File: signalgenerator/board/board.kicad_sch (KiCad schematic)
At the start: 20 parts, among them U1 MachXO2-1200, U5 74LVC04, U6 STLQ015M33R

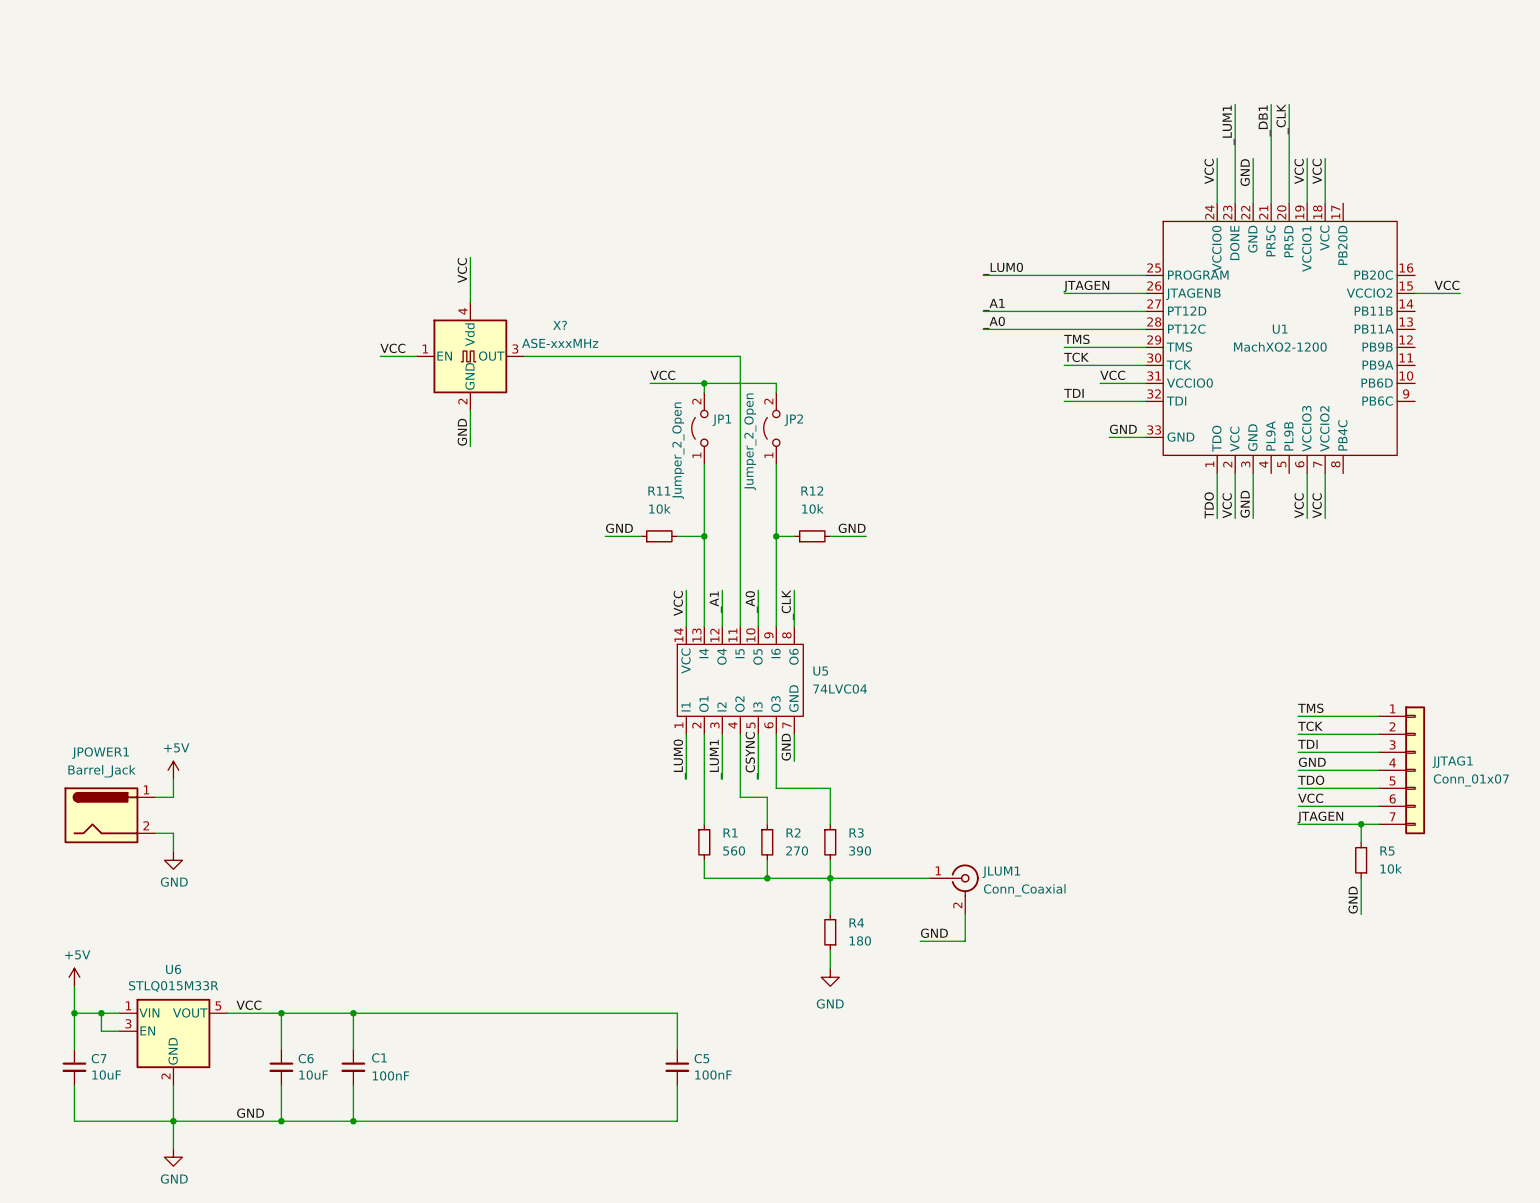
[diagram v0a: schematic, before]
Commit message: Reference board schematic
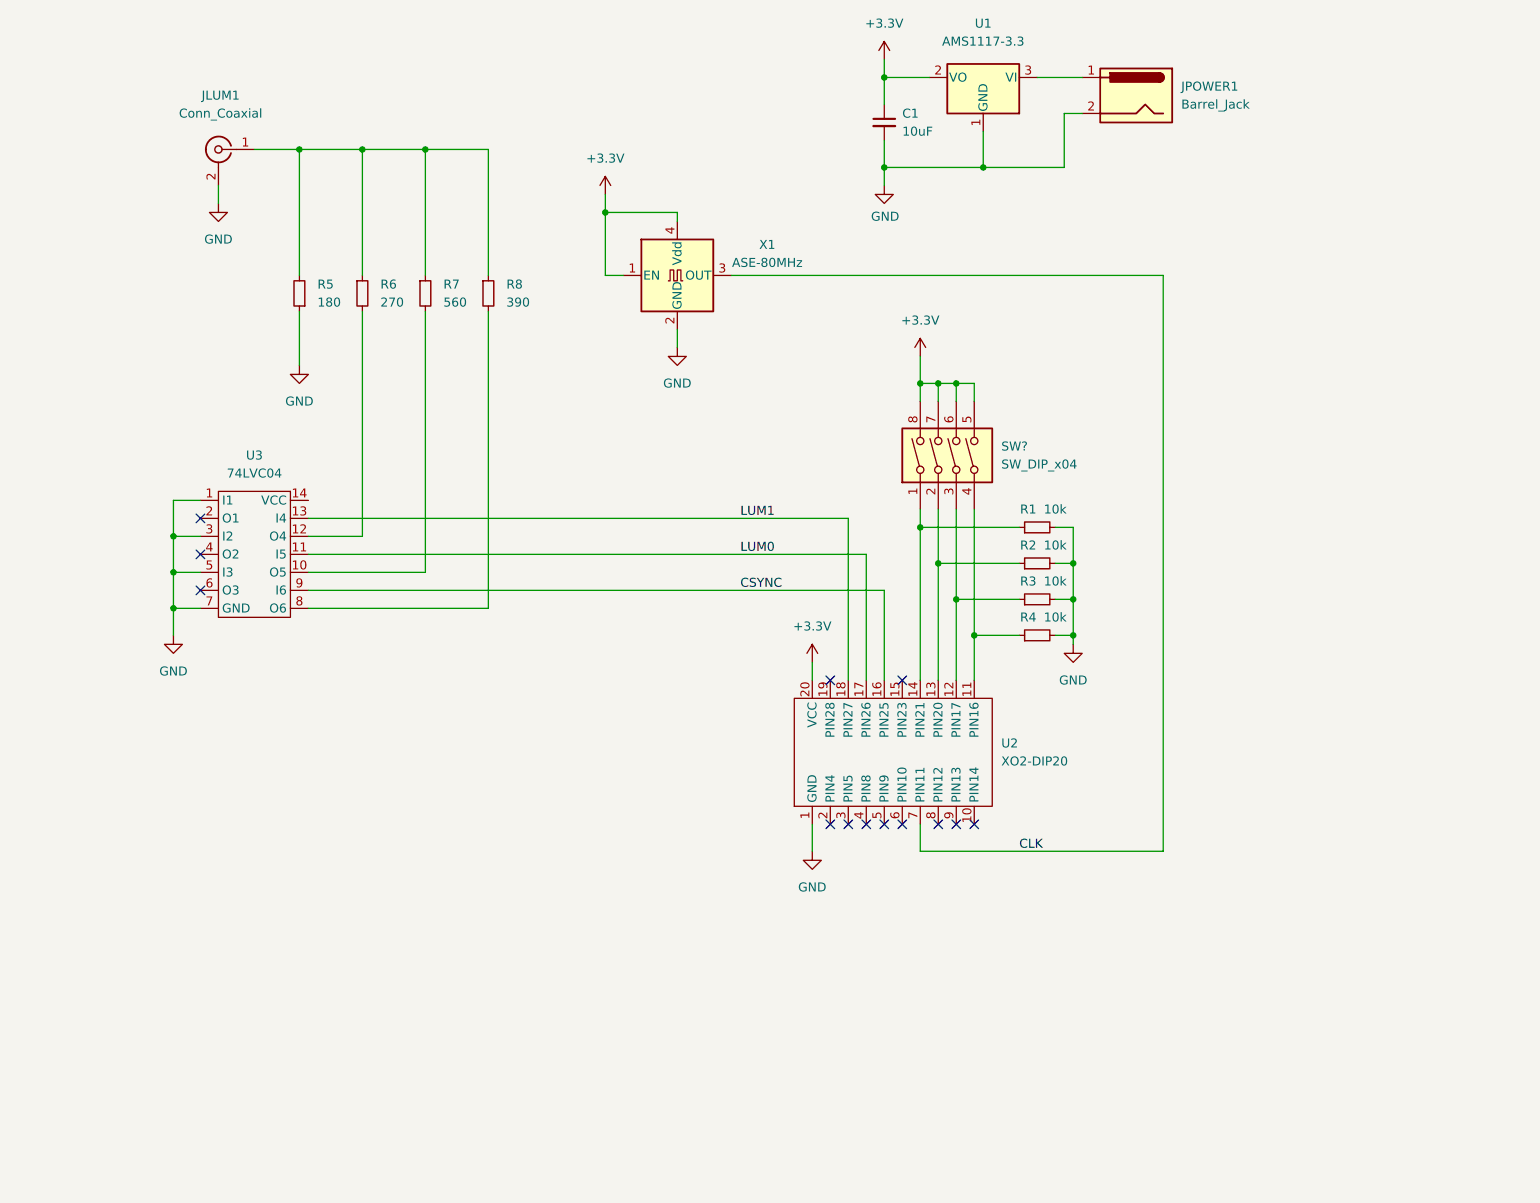
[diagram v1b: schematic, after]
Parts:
- removed C5: 100nF, Capacitor_SMD:C_0603_1608Metric, symbol Device:C_Small
- removed C6, C7: 10uF, Capacitor_SMD:C_0805_2012Metric, symbol Device:C_Small
- removed JJTAG1: Conn_01x07, Connector_PinHeader_2.54mm:PinHeader_1x07_P2.54mm_Vertical, symbol Connector_Generic:Conn_01x07
- removed JP1, JP2: Jumper_2_Open, symbol Jumper:Jumper_2_Open
- removed R11, R12: 10k, symbol Device:R_Small
- removed R5: 10k, Resistor_SMD:R_0805_2012Metric_Pad1.20x1.40mm_HandSolder, symbol Device:R_Small
- removed U1: MachXO2-1200, footprints:QFN-32-1EP_5x5mm_P0.5mm_EP3.1x3.1mm_ThermalVias, symbol Library:MachXO2-1200
- removed U6: STLQ015M33R, Package_TO_SOT_SMD:SOT-23-5, symbol vicboard-rescue:AP2127K-3.3-Regulator_Linear
- added R1, R2, R3, R4: 10k, symbol Device:R_Small
- added SW?: SW_DIP_x04, symbol Switch:SW_DIP_x04
- added U1: AMS1117-3.3, Package_TO_SOT_SMD:SOT-223-3_TabPin2, symbol Regulator_Linear:AMS1117-3.3
- added U2: XO2-DIP20, symbol Library:XO2-DIP20
- C1: value 100nF -> 10uF; footprint Capacitor_SMD:C_0603_1608Metric -> (none)
- X1: renamed from X?; value ASE-xxxMHz -> ASE-80MHz
- renumbered R4 to R5, R2 to R6, R1 to R7, R3 to R8, U5 to U3
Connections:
- net _CSYNC is gone; now on net GND: U3.5 (I3)
- net _LUM0 is gone; now on net GND: U3.1 (I1)
- net _LUM1 is gone; now on net GND: U3.3 (I2)
- net GND: now also R1.2, R2.2, R3.2, R4.2, U1.1 (GND), U2.1 (GND)
- net LUM1: now reaches U3.13 (I4)
- net LUM1: now also U2.18 (PIN27)
- net CLK: now reaches X1.3 (OUT)
- net CLK: now also U2.7 (PIN11); no longer U3.11 (I5)
- net at U3.2 (O1): no longer R7.1
- net at U3.4 (O2): no longer R6.1
- net at U3.6 (O3): no longer R8.1
- net CSYNC: now reaches U3.9 (I6)
- net CSYNC: now also U2.16 (PIN25)
- net +5V: no longer names the net of JPOWER1.1
- net +5V: now also U1.3 (VI)
- net VCC renamed +3.3V
- net +3.3V: now also SW?.5, SW?.6, SW?.7, SW?.8, U1.2 (VO), U2.20 (VCC); no longer U3.14 (VCC)
- net _A0: no longer names the net of U3.10 (O5)
- net _A0: now also R7.2
- net _A1: no longer names the net of U3.12 (O4)
- net _A1: now also R6.2
- net _CLK: no longer names the net of U3.8 (O6)
- net _CLK: now also R8.2
- new net: R4.1, SW?.4, U2.11 (PIN16)
- new net: R3.1, SW?.3, U2.12 (PIN17)
- new net: R2.1, SW?.2, U2.13 (PIN20)
- new net: R1.1, SW?.1, U2.14 (PIN21)
- new net: JLUM1.1 (In), R5.2, R6.1, R7.1, R8.1
- new net LUM0: U2.17 (PIN26), U3.11 (I5)
- no-connect marks 0 -> 13
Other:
- moved on the sheet: JLUM1, JPOWER1, R5, R6, R7, R8, U3, X1

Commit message: PCB for signal generator
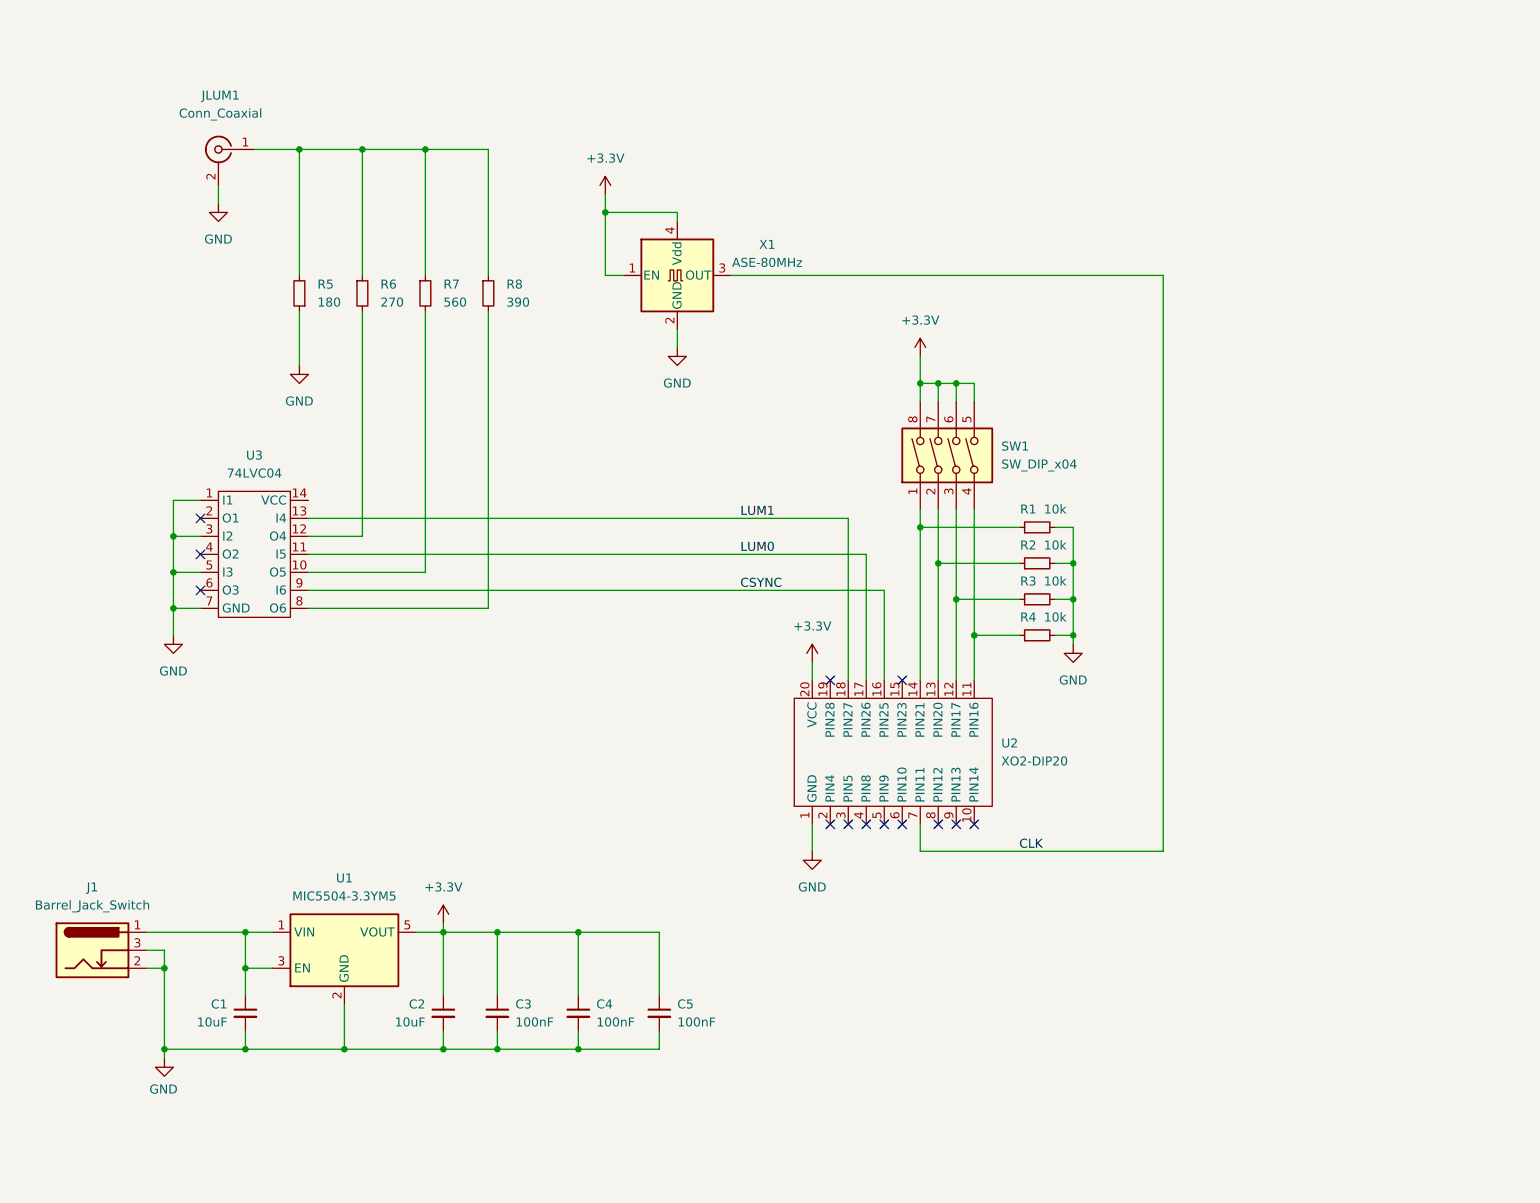
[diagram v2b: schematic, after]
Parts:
- removed JPOWER1: Barrel_Jack, symbol Connector:Barrel_Jack
- removed U1: AMS1117-3.3, Package_TO_SOT_SMD:SOT-223-3_TabPin2, symbol Regulator_Linear:AMS1117-3.3
- added C2: 10uF, Capacitor_SMD:C_0805_2012Metric_Pad1.18x1.45mm_HandSolder, symbol Device:C_Small
- added C3, C4, C5: 100nF, Capacitor_SMD:C_0603_1608Metric_Pad1.08x0.95mm_HandSolder, symbol Device:C_Small
- added J1: Barrel_Jack_Switch, Connector_BarrelJack:BarrelJack_Horizontal, symbol Connector:Barrel_Jack_Switch
- added U1: MIC5504-3.3YM5, Package_TO_SOT_SMD:SOT-23-5, symbol Regulator_Linear:MIC5504-3.3YM5
- C1: footprint (none) -> Capacitor_SMD:C_0805_2012Metric_Pad1.18x1.45mm_HandSolder
- JLUM1: footprint (none) -> Projectfootprints:RCA_JACK
- R1, R2, R3, R4: footprint (none) -> Resistor_SMD:R_0805_2012Metric_Pad1.20x1.40mm_HandSolder
- SW1: renamed from SW?; footprint (none) -> Package_DIP:DIP-8_W7.62mm
- U2: footprint (none) -> Package_DIP:DIP-20_W7.62mm
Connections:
- net +3.3V: now also C2.1, C3.1, C4.1, C5.1, U1.5 (VOUT); no longer C1.1
- net GND: now also C2.2, C3.2, C4.2, C5.2, J1.2, J1.3, U1.2 (GND)
- new net: C1.1, J1.1, U1.1 (VIN), U1.3 (EN)
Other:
- moved on the sheet: C1

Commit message: Implement NES signal PAL/NTSC
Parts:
- removed C5: 100nF, Capacitor_SMD:C_0603_1608Metric_Pad1.08x0.95mm_HandSolder, symbol Device:C_Small
- removed U1: MIC5504-3.3YM5, Package_TO_SOT_SMD:SOT-23-5, symbol Regulator_Linear:MIC5504-3.3YM5
- removed X1: ASE-80MHz, Oscillator:Oscillator_SMD_Abracon_ASE-4Pin_3.2x2.5mm, symbol Oscillator:ASE-xxxMHz
- added U1: AMS1117-3.3, Package_TO_SOT_SMD:SOT-223-3_TabPin2, symbol Regulator_Linear:AMS1117-3.3
- added X2: XO53, Oscillator:Oscillator_SMD_EuroQuartz_XO53-4Pin_5.0x3.2mm, symbol Oscillator:XO53
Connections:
- net +3.3V: now also U3.14 (VCC), U1.2 (VO), X2.1 (EN), X2.4 (V+)
- net CLK: now also X2.3 (OUT)
- net GND: now also U1.1 (GND), X2.2 (GND)
- net at C1.1, J1.1: now also U1.3 (VI)

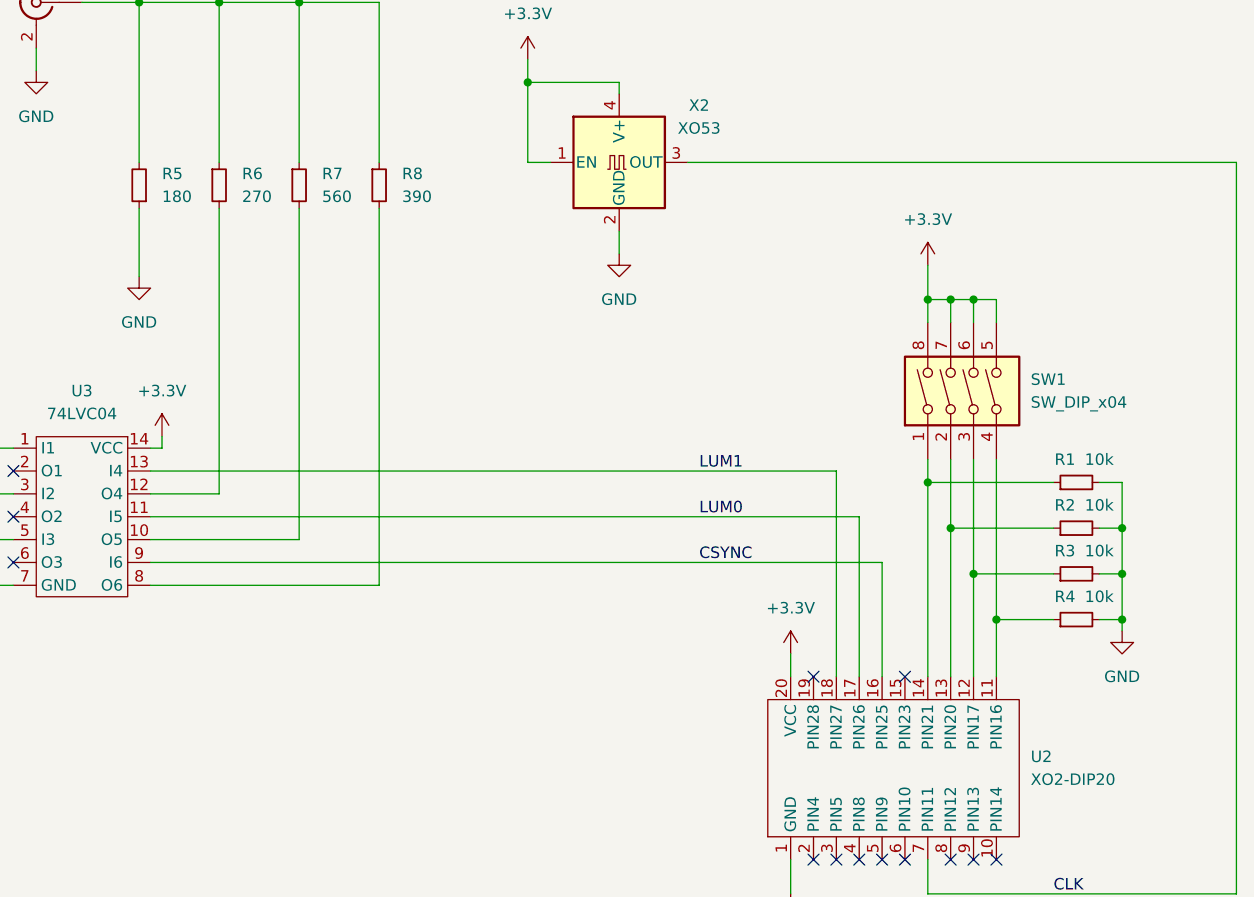
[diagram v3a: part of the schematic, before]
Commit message: Implement XOR sync in signal pattern
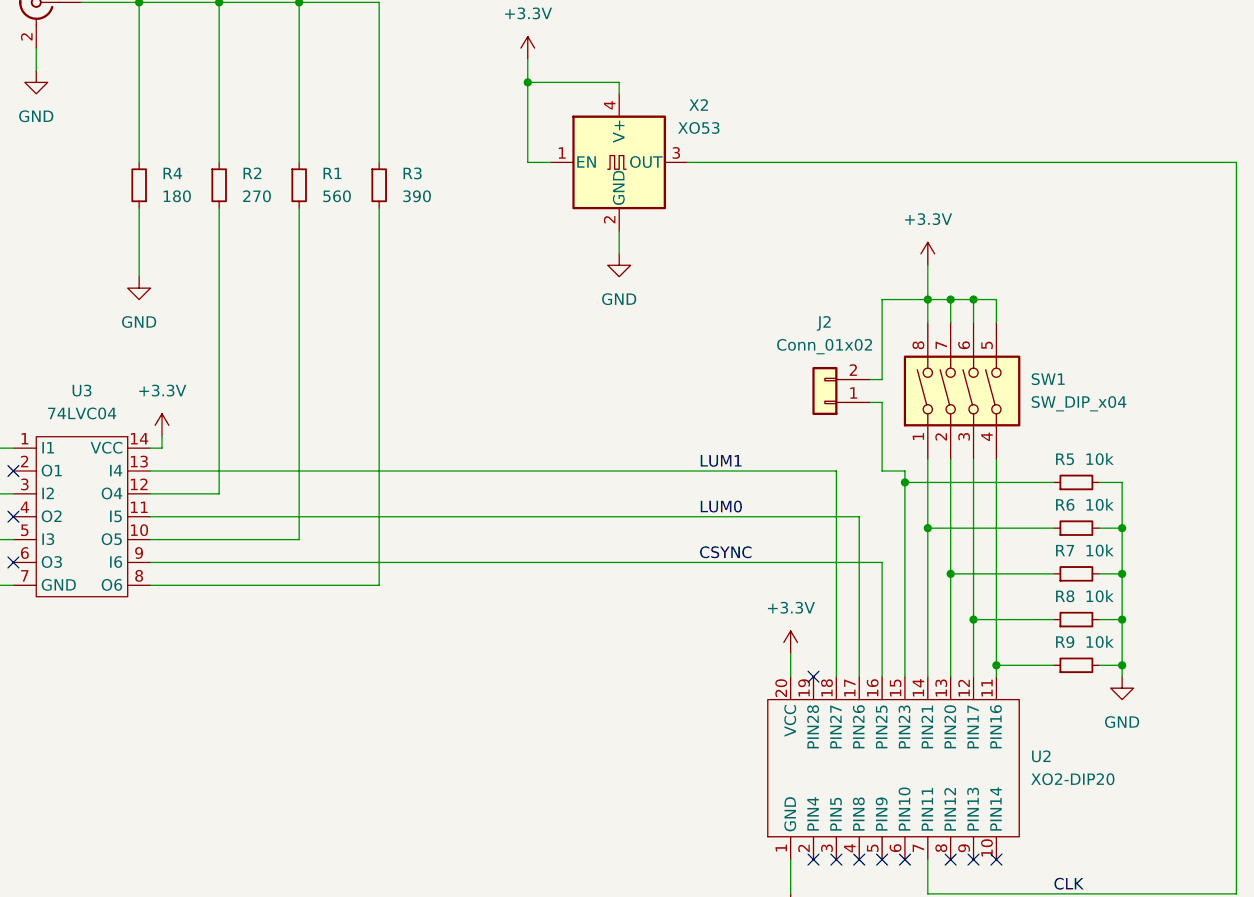
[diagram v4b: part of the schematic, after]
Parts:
- added J2: Conn_01x02, symbol Connector_Generic:Conn_01x02
- added R5: 10k, Resistor_SMD:R_0805_2012Metric_Pad1.20x1.40mm_HandSolder, symbol Device:R_Small
- renumbered R7 to R1, R6 to R2, R8 to R3, R5 to R4, R1 to R6, R2 to R7, R3 to R8, R4 to R9
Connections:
- net +3.3V: now also J2.2 (Pin_2)
- net GND: now also R5.2
- net at U2.15 (PIN23): now also J2.1 (Pin_1), R5.1
- no-connect marks 13 -> 12
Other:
- moved on the sheet: R6, R7, R8, R9
